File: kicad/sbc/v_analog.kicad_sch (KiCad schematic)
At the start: 30 parts, among them J2 RGB, J4 S-VIDEO, U12 cxa2075M, X1 OSC

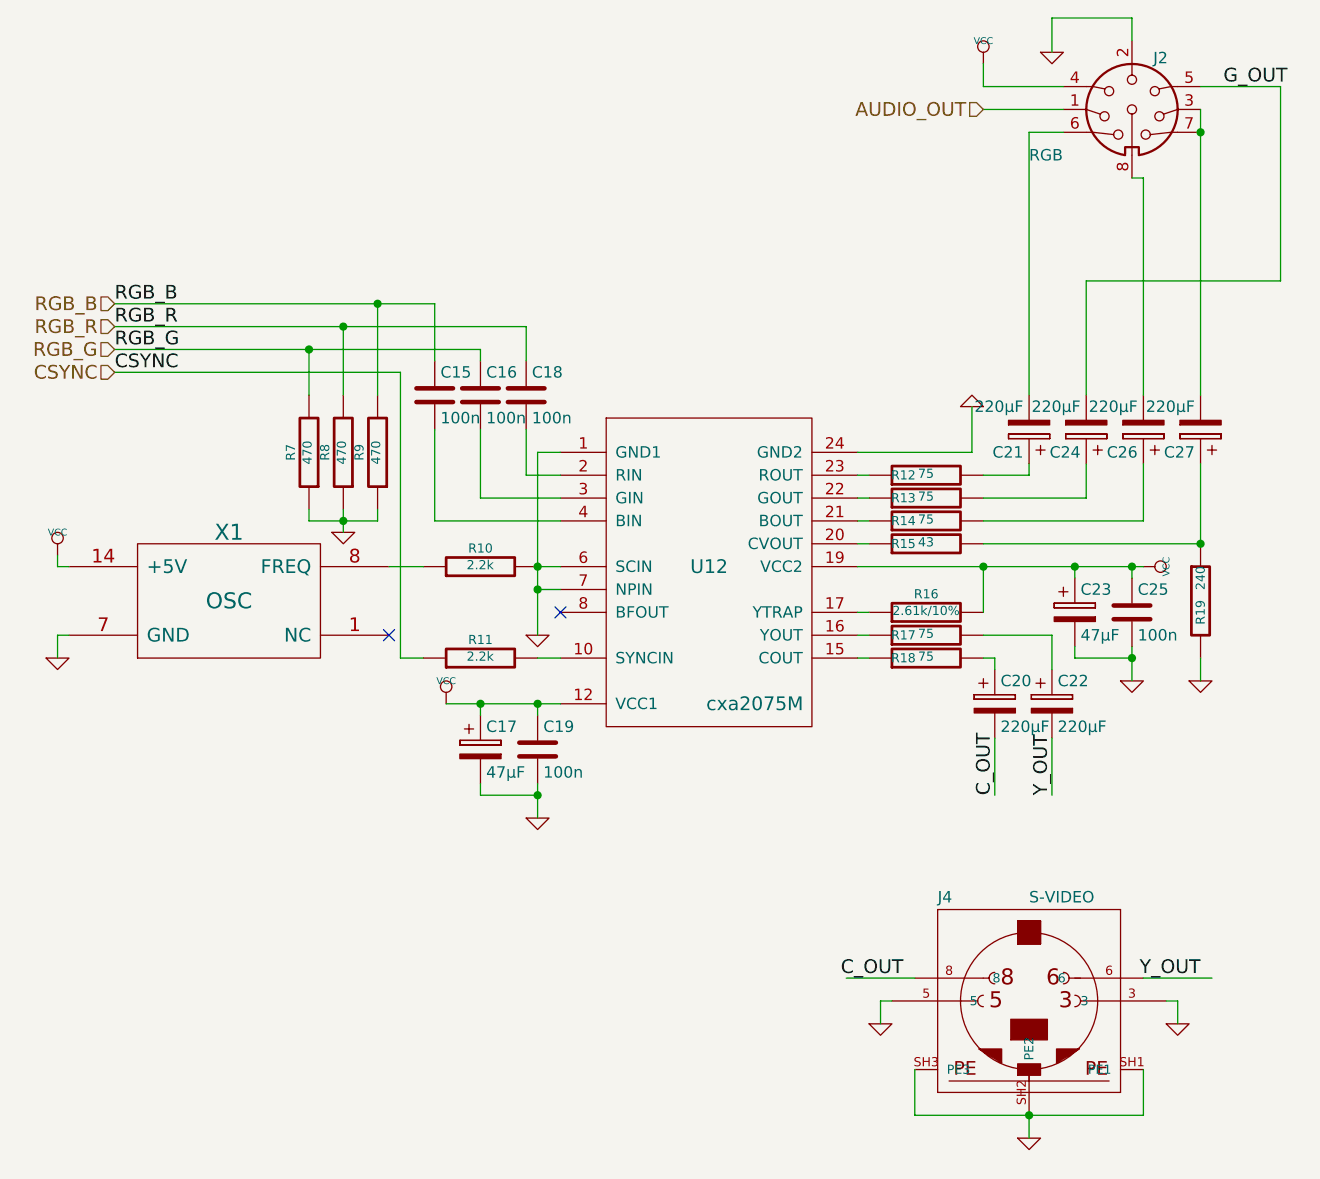
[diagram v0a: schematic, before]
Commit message: fix ERC messages
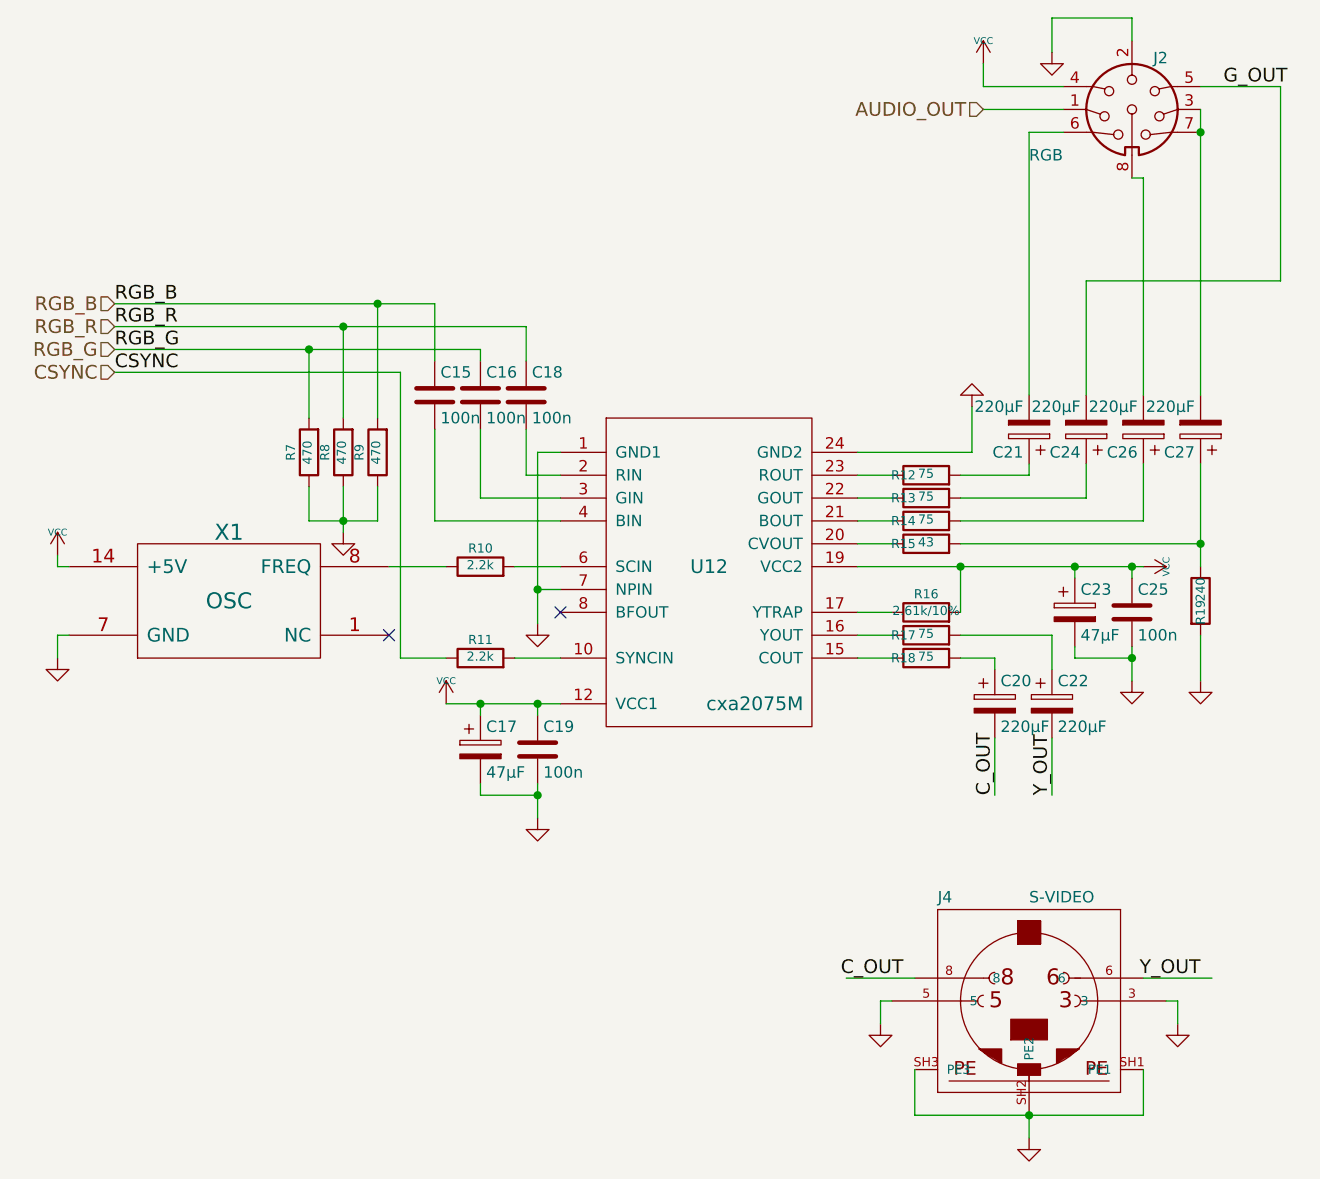
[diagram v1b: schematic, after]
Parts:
- C15, C16, C18, C19, C25: symbol v9958-rescue:C -> Device:C
- C17, C20, C21, C22, C23, C24, C26, C27: symbol v9958-rescue:CP -> Device:C_Polarized
- R10, R11, R12, R13, R14, R15, R16, R17, R18, R19, R7, R8, R9: symbol v9958-rescue:R-RESCUE-v9958 -> Device:R
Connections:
- net GND: no longer R10.2, U12.6 (SCIN)
- new net: R10.2, U12.6 (SCIN)

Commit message: cleanup ERC warnings and errors
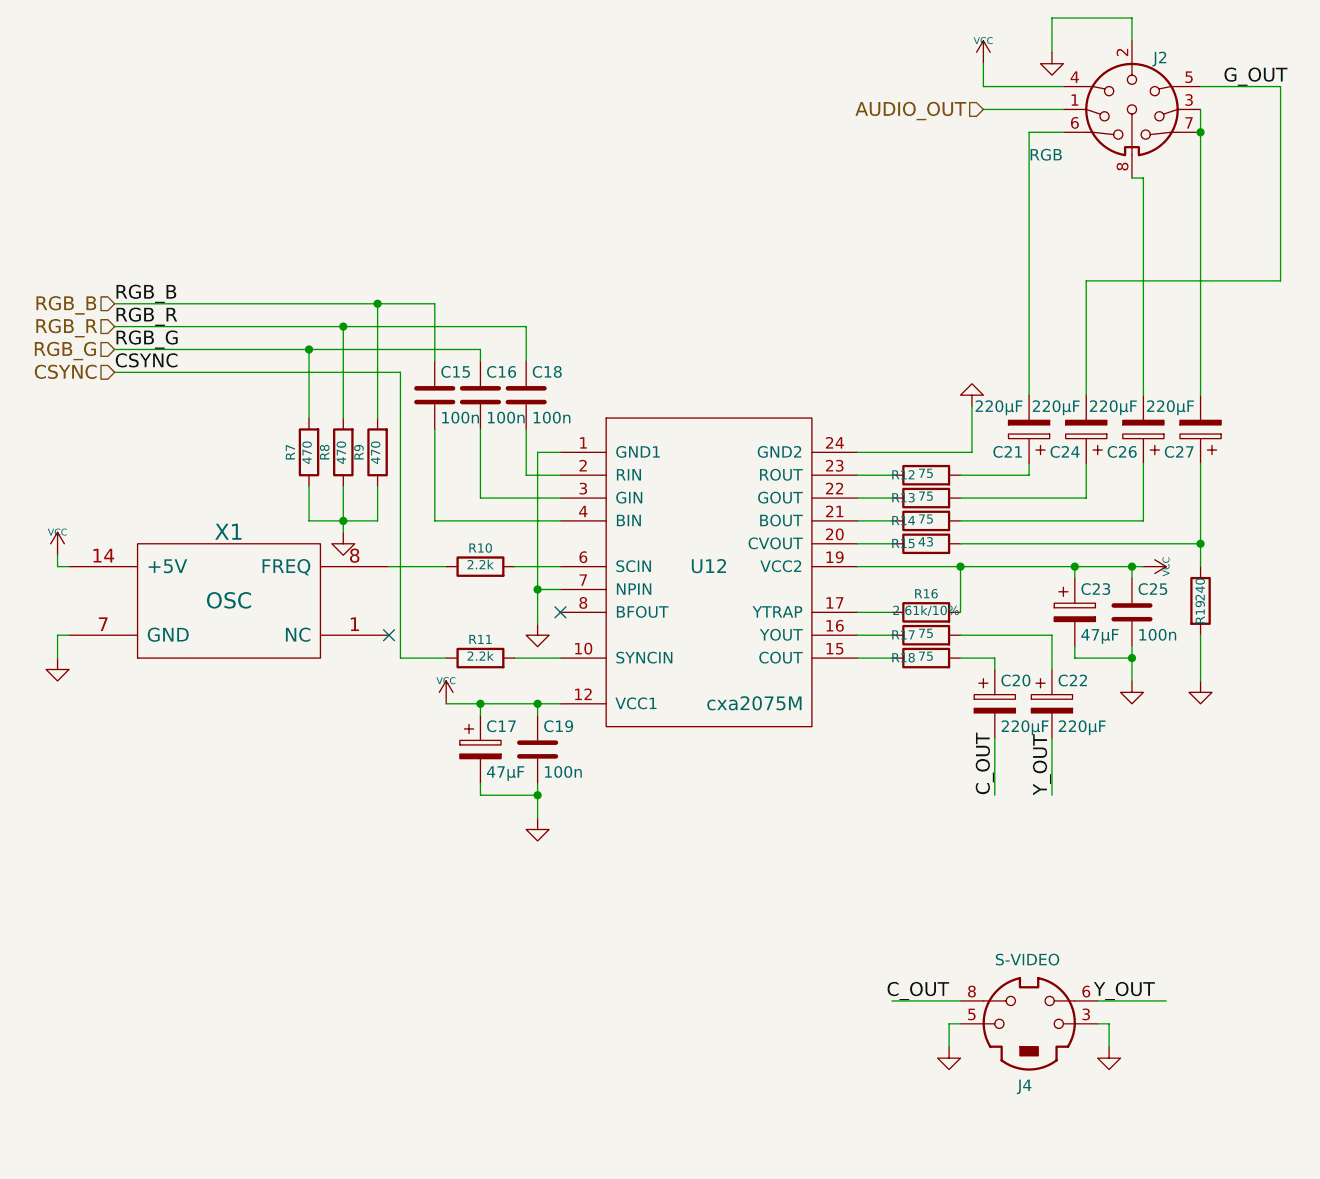
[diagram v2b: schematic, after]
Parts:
- J2: symbol v9958-rescue:DIN-8 -> Connector:DIN-8
- J4: symbol v9958-rescue:MINI_DIN_4 -> Connector:Mini-DIN-4
- U12: symbol v9958-rescue:cxa2075M -> tms99x:cxa2075M
- X1: symbol v9958-rescue:OSC -> osc:OSC
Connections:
- net GND: no longer J4.SH1 (PE1), J4.SH2 (PE2), J4.SH3 (PE3)
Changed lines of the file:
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@@
   (junction (at 100.33 87.63) (diameter 0) (color 0 0 0 0)
-  )
-  (junction (at 176.53 153.67) (diameter 0) (color 0 0 0 0)
   )
   (junction (at 168.91 92.71) (diameter 0) (color 0 0 0 0)
@@
     (stroke (width 0) (type default))
   )
-  (wire (pts (xy 160.02 140.97) (xy 161.29 140.97))
+  (wire (pts (xy 167.64 143.51) (xy 168.91 143.51))
     (stroke (width 0) (type default))
   )
@@
     (stroke (width 0) (type default))
   )
-  (wire (pts (xy 193.04 140.97) (xy 193.04 143.51))
+  (wire (pts (xy 185.42 143.51) (xy 185.42 146.05))
     (stroke (width 0) (type default))
   )
@@
     (stroke (width 0) (type default))
   )
-  (wire (pts (xy 176.53 153.67) (xy 176.53 156.21))
-    (stroke (width 0) (type default))
-  )
   (wire (pts (xy 119.38 92.71) (xy 124.46 92.71))
     (stroke (width 0) (type default))
@@
     (stroke (width 0) (type default))
   )
-  (wire (pts (xy 176.53 153.67) (xy 189.23 153.67))
-    (stroke (width 0) (type default))
-  )
   (wire (pts (xy 74.93 63.5) (xy 104.14 63.5))
     (stroke (width 0) (type default))
@@
     (stroke (width 0) (type default))
   )
-  (wire (pts (xy 189.23 153.67) (xy 189.23 148.59))
-    (stroke (width 0) (type default))
-  )
   (wire (pts (xy 168.91 97.79) (xy 168.91 92.71))
     (stroke (width 0) (type default))
@@
     (stroke (width 0) (type default))
   )
-  (wire (pts (xy 163.83 148.59) (xy 163.83 153.67))
-    (stroke (width 0) (type default))
-  )
   (wire (pts (xy 181.61 92.71) (xy 187.96 92.71))
     (stroke (width 0) (type default))
@@
     (stroke (width 0) (type default))
   )
-  (wire (pts (xy 189.23 138.43) (xy 196.85 138.43))
+  (wire (pts (xy 184.15 140.97) (xy 191.77 140.97))
     (stroke (width 0) (type default))
   )
@@
     (stroke (width 0) (type default))
   )
-  (wire (pts (xy 163.83 153.67) (xy 176.53 153.67))
-    (stroke (width 0) (type default))
-  )
   (wire (pts (xy 176.53 82.55) (xy 176.53 81.28))
     (stroke (width 0) (type default))
@@
     (stroke (width 0) (type default))
   )
-  (wire (pts (xy 163.83 138.43) (xy 156.21 138.43))
+  (wire (pts (xy 168.91 140.97) (xy 161.29 140.97))
     (stroke (width 0) (type default))
   )
@@
     (stroke (width 0) (type default))
   )
-  (wire (pts (xy 160.02 143.51) (xy 160.02 140.97))
+  (wire (pts (xy 167.64 146.05) (xy 167.64 143.51))
     (stroke (width 0) (type default))
   )
@@
     (stroke (width 0) (type default))
   )
-  (wire (pts (xy 191.77 140.97) (xy 193.04 140.97))
+  (wire (pts (xy 184.15 143.51) (xy 185.42 143.51))
     (stroke (width 0) (type default))
   )
@@
     (effects (font (size 1.524 1.524)) (justify left bottom))
   )
-  (label "C_OUT" (at 162.56 138.43 180) (fields_autoplaced)
+  (label "C_OUT" (at 167.64 140.97 180) (fields_autoplaced)
     (effects (font (size 1.524 1.524)) (justify right bottom))
   )
@@
     (effects (font (size 1.524 1.524)) (justify left bottom))
   )
-  (label "Y_OUT" (at 195.58 138.43 180) (fields_autoplaced)
+  (label "Y_OUT" (at 190.5 140.97 180) (fields_autoplaced)
     (effects (font (size 1.524 1.524)) (justify right bottom))
   )
@@
     (effects (font (size 1.524 1.524)) (justify right))
   )
-  (symbol (lib_id "v9958-rescue:OSC") (at 87.63 96.52 0) (unit 1)
+  (symbol (lib_id "osc:OSC") (at 87.63 96.52 0) (unit 1)
     (in_bom yes) (on_board yes) (dnp no)
     (property "Reference" "X1" (at 87.63 88.9 0)
@@
     )
   )
-  (symbol (lib_id "power:GND") (at 193.04 143.51 0) (unit 1)
-    (in_bom yes) (on_board yes) (dnp no)
-    (property "Reference" "#PWR052" (at 193.04 143.51 0)
-      (effects (font (size 0.762 0.762)) hide)
-    )
-    (property "Value" "GND" (at 193.04 145.288 0)
-      (effects (font (size 0.762 0.762)) hide)
-    )
-    (property "Footprint" "" (at 193.04 143.51 0)
-      (effects (font (size 1.27 1.27)) hide)
-    )
-    (property "Datasheet" "" (at 193.04 143.51 0)
+  (symbol (lib_id "power:GND") (at 185.42 146.05 0) (unit 1)
+    (in_bom yes) (on_board yes) (dnp no)
+    (property "Reference" "#PWR052" (at 185.42 146.05 0)
+      (effects (font (size 0.762 0.762)) hide)
+    )
+    (property "Value" "GND" (at 185.42 147.828 0)
+      (effects (font (size 0.762 0.762)) hide)
+    )
+    (property "Footprint" "" (at 185.42 146.05 0)
+      (effects (font (size 1.27 1.27)) hide)
+    )
+    (property "Datasheet" "" (at 185.42 146.05 0)
       (effects (font (size 1.27 1.27)) hide)
     )
@@
     )
   )
-  (symbol (lib_id "power:GND") (at 160.02 143.51 0) (unit 1)
-    (in_bom yes) (on_board yes) (dnp no)
-    (property "Reference" "#PWR051" (at 160.02 143.51 0)
-      (effects (font (size 0.762 0.762)) hide)
-    )
-    (property "Value" "GND" (at 160.02 145.288 0)
-      (effects (font (size 0.762 0.762)) hide)
-    )
-    (property "Footprint" "" (at 160.02 143.51 0)
-      (effects (font (size 1.27 1.27)) hide)
-    )
-    (property "Datasheet" "" (at 160.02 143.51 0)
+  (symbol (lib_id "power:GND") (at 167.64 146.05 0) (unit 1)
+    (in_bom yes) (on_board yes) (dnp no)
+    (property "Reference" "#PWR051" (at 167.64 146.05 0)
+      (effects (font (size 0.762 0.762)) hide)
+    )
+    (property "Value" "GND" (at 167.64 147.828 0)
+      (effects (font (size 0.762 0.762)) hide)
+    )
+    (property "Footprint" "" (at 167.64 146.05 0)
+      (effects (font (size 1.27 1.27)) hide)
+    )
+    (property "Datasheet" "" (at 167.64 146.05 0)
       (effects (font (size 1.27 1.27)) hide)
     )
@@
     )
   )
-  (symbol (lib_id "v9958-rescue:cxa2075M") (at 140.97 92.71 0) (unit 1)
+  (symbol (lib_id "tms99x:cxa2075M") (at 140.97 92.71 0) (unit 1)
     (in_bom yes) (on_board yes) (dnp no)
     (property "Reference" "U12" (at 140.97 92.71 0)
@@
     )
   )
-  (symbol (lib_id "v9958-rescue:MINI_DIN_4") (at 176.53 143.51 0) (unit 1)
-    (in_bom yes) (on_board yes) (dnp no)
-    (property "Reference" "J4" (at 166.37 130.175 0)
+  (symbol (lib_id "Connector:Mini-DIN-4") (at 176.53 143.51 0) (unit 1)
+    (in_bom yes) (on_board yes) (dnp no)
+    (property "Reference" "J4" (at 175.26 151.13 0)
       (effects (font (size 1.27 1.27)) (justify left bottom))
     )
-    (property "Value" "S-VIDEO" (at 176.53 130.175 0)
+    (property "Value" "S-VIDEO" (at 172.72 137.16 0)
       (effects (font (size 1.27 1.27)) (justify left bottom))
     )
-    (property "Footprint" "DIN:mini_din-M_DIN4" (at 176.53 139.7 0)
-      (effects (font (size 1.27 1.27)) hide)
-    )
-    (property "Datasheet" "" (at 176.53 143.51 0)
-      (effects (font (size 1.524 1.524)))
+    (property "Footprint" "DIN:mini_din-M_DIN4" (at 176.53 146.05 0)
+      (effects (font (size 1.27 1.27)) hide)
+    )
+    (property "Datasheet" "http://service.powerdynamics.com/ec/Catalog17/Section%2011.pdf" (at 176.53 148.59 0)
+      (effects (font (size 1.27 1.27)) hide)
     )
     (pin "3")
@@
     (pin "6")
     (pin "8")
-    (pin "SH1")
-    (pin "SH2")
-    (pin "SH3")
     (instances
       (project "v9958"
@@
     )
   )
-  (symbol (lib_id "power:GND") (at 176.53 156.21 0) (unit 1)
-    (in_bom yes) (on_board yes) (dnp no)
-    (property "Reference" "#PWR053" (at 176.53 156.21 0)
-      (effects (font (size 0.762 0.762)) hide)
-    )
-    (property "Value" "GND" (at 176.53 157.988 0)
-      (effects (font (size 0.762 0.762)) hide)
-    )
-    (property "Footprint" "" (at 176.53 156.21 0)
-      (effects (font (size 1.27 1.27)) hide)
-    )
-    (property "Datasheet" "" (at 176.53 156.21 0)
-      (effects (font (size 1.27 1.27)) hide)
-    )
-    (pin "1")
-    (instances
-      (project "v9958"
-        (path "/8677aa04-d5f3-4ab1-a2c2-991cda76ac9e/00000000-0000-0000-0000-00005be2b3f4"
-          (reference "#PWR053") (unit 1)
-        )
-      )
-      (project "sbc"
-        (path "/896d5dab-44ec-47d0-8232-7ef57773545e/28a4b651-8375-4e62-9061-4149cd570bf0/731cd2f3-5c05-4e00-bfb3-627f05512aca"
-          (reference "#PWR057") (unit 1)
-        )
-      )
-    )
-  )
-  (symbol (lib_id "v9958-rescue:DIN-8") (at 187.96 41.91 0) (unit 1)
+  (symbol (lib_id "Connector:DIN-8") (at 187.96 41.91 0) (unit 1)
     (in_bom yes) (on_board yes) (dnp no)
     (property "Reference" "J2" (at 191.135 36.195 0)
@@
       (effects (font (size 1.27 1.27)) hide)
     )
-    (property "Datasheet" "" (at 187.96 41.91 0)
-      (effects (font (size 1.27 1.27)) hide)
-    )
+    (property "Datasheet" "http://www.mouser.com/ds/2/18/40_c091_abd_e-75918.pdf" (at 187.96 41.91 0)
+      (effects (font (size 1.27 1.27)) hide)
+    )

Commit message: regular sd socket separate masses for analog and digital cleanup routing
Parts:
- C20, C21, C22, C24, C26, C27: footprint Capacitor_THT:CP_Radial_D4.0mm_P2.00mm -> Capacitor_THT:CP_Radial_D6.3mm_P2.50mm
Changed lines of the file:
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@@
       (effects (font (size 1.27 1.27)) (justify left))
     )
-    (property "Footprint" "Capacitor_THT:CP_Radial_D4.0mm_P2.00mm" (at 180.0352 111.76 0)
+    (property "Footprint" "Capacitor_THT:CP_Radial_D6.3mm_P2.50mm" (at 180.0352 111.76 0)
       (effects (font (size 1.27 1.27)) hide)
     )
@@
       (effects (font (size 1.27 1.27)) (justify left))
     )
-    (property "Footprint" "Capacitor_THT:CP_Radial_D4.0mm_P2.00mm" (at 173.6852 111.76 0)
+    (property "Footprint" "Capacitor_THT:CP_Radial_D6.3mm_P2.50mm" (at 173.6852 111.76 0)
       (effects (font (size 1.27 1.27)) hide)
     )
@@
       (effects (font (size 1.27 1.27)) (justify left))
     )
-    (property "Footprint" "Capacitor_THT:CP_Radial_D4.0mm_P2.00mm" (at 175.5648 73.66 0)
+    (property "Footprint" "Capacitor_THT:CP_Radial_D6.3mm_P2.50mm" (at 175.5648 73.66 0)
       (effects (font (size 1.27 1.27)) hide)
     )
@@
       (effects (font (size 1.27 1.27)) (justify left))
     )
-    (property "Footprint" "Capacitor_THT:CP_Radial_D4.0mm_P2.00mm" (at 194.6148 73.66 0)
+    (property "Footprint" "Capacitor_THT:CP_Radial_D6.3mm_P2.50mm" (at 194.6148 73.66 0)
       (effects (font (size 1.27 1.27)) hide)
     )
@@
       (effects (font (size 1.27 1.27)) (justify left))
     )
-    (property "Footprint" "Capacitor_THT:CP_Radial_D4.0mm_P2.00mm" (at 181.9148 73.66 0)
+    (property "Footprint" "Capacitor_THT:CP_Radial_D6.3mm_P2.50mm" (at 181.9148 73.66 0)
       (effects (font (size 1.27 1.27)) hide)
     )
@@
       (effects (font (size 1.27 1.27)) (justify left))
     )
-    (property "Footprint" "Capacitor_THT:CP_Radial_D4.0mm_P2.00mm" (at 188.2648 73.66 0)
-      (effects (font (size 1.27 1.27)) hide)
-    )
+    (property "Footprint" "Capacitor_THT:CP_Radial_D6.3mm_P2.50mm" (at 188.2648 73.66 0)
+      (effects (font (size 1.27 1.27)) hide)
+    )

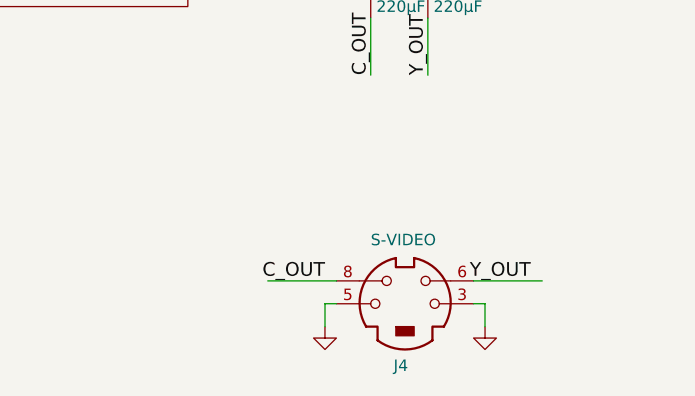
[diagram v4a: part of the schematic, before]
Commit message: better s-video jack footprint
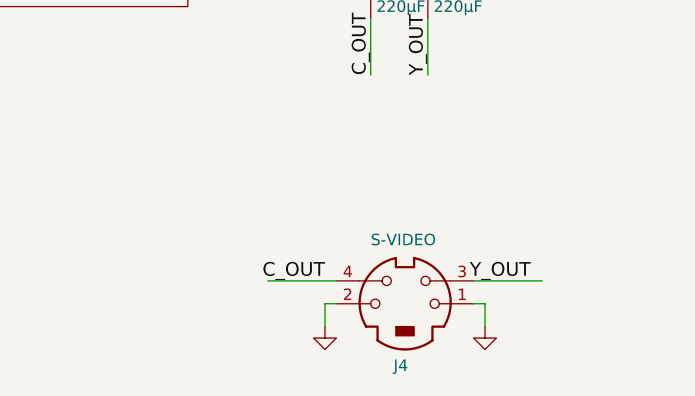
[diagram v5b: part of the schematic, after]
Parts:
- J4: footprint DIN:mini_din-M_DIN4 -> minidin:Mini_DIN_4_TE_Connectivity
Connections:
- net C_OUT: now also J4.4; no longer J4.8
- net GND: now also J4.1, J4.2; no longer J4.3, J4.5
- net Y_OUT: now also J4.3; no longer J4.6
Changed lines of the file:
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@@
       (effects (font (size 1.27 1.27)) (justify left bottom))
     )
-    (property "Footprint" "DIN:mini_din-M_DIN4" (at 176.53 146.05 0)
+    (property "Footprint" "minidin:Mini_DIN_4_TE_Connectivity" (at 176.53 146.05 0)
       (effects (font (size 1.27 1.27)) hide)
     )
@@
       (effects (font (size 1.27 1.27)) hide)
     )
+    (pin "1")
+    (pin "2")
     (pin "3")
-    (pin "5")
-    (pin "6")
-    (pin "8")
+    (pin "4")
     (instances
       (project "v9958"
